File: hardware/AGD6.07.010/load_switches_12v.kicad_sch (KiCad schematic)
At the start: 0 parts

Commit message: Draw full AGD6.07.010 schematic per integrated_avionics_board spec
All ten sheets now carry components: 14S input with hot-swap and power
monitor, 12/5/3.3 V rails and a separate 12 V AI channel with soft-start
and current telemetry, Pixhawk connectors, CAN1/CAN2 hub with chokes,
ESD and switchable termination, sensor conditioning, SIYI and radar,
AI interface and watchdog, protected 12 V switches with diagnostics,
fan/heater control, cameras and Ethernet. Open choices are recorded in
DECISIONS.md; datasheet-dependent values are flagged CHECK_DATASHEET.

ERC: no errors. All 752 intended pin connections match the KiCad netlist.

Co-Authored-By: Claude Opus 5.5 <noreply@anthropic.com>
Claude-Session: https://claude.ai/code/session_01Qk7uTKdi6YbndB9fGuguYV
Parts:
- added C804, C811, C821, C831: 100n, Capacitor_SMD:C_0402_1005Metric, symbol Device:C
- added C805: 10u 25V, Capacitor_SMD:C_1210_3225Metric, symbol Device:C
- added D801, D802, D803, D804, D805: SS14, Diode_SMD:D_SMA, symbol Diode:SS14
- added D806: ESD9B5.0ST5G, Diode_SMD:D_SOD-923, symbol Diode:ESD9B5.0ST5G
- added D807: BAT54C, Package_TO_SOT_SMD:SOT-23, symbol Diode:BAT54C
- added F801: 0.5A, Fuse:Fuse_1206_3216Metric, symbol Device:Polyfuse
- added F802: 1.5A, Fuse:Fuse_1812_4532Metric, symbol Device:Polyfuse
- added J801: VALVE1 XH2, Connector_JST:JST_XH_B2B-XH-A_1x02_P2.50mm_Vertical, symbol Connector_Generic:Conn_01x02
- added J802: VALVE2 XH2, Connector_JST:JST_XH_B2B-XH-A_1x02_P2.50mm_Vertical, symbol Connector_Generic:Conn_01x02
- added J803: LIGHTS XH2, Connector_JST:JST_XH_B2B-XH-A_1x02_P2.50mm_Vertical, symbol Connector_Generic:Conn_01x02
- added J804: FAN XH2, Connector_JST:JST_XH_B2B-XH-A_1x02_P2.50mm_Vertical, symbol Connector_Generic:Conn_01x02
- added J805: HEATER XH2, Connector_JST:JST_XH_B2B-XH-A_1x02_P2.50mm_Vertical, symbol Connector_Generic:Conn_01x02
- added J806: PUMP_ESC_SIG GH3, Connector_JST:JST_GH_SM03B-GHS-TB_1x03-1MP_P1.25mm_Horizontal, symbol Connector_Generic:Conn_01x03
- added Q801, Q803: AO3400A, Package_TO_SOT_SMD:SOT-23, symbol Transistor_FET:AO3400A
- added Q802: AO3401A, Package_TO_SOT_SMD:SOT-23, symbol Transistor_FET:AO3401A
- added R804, R811, R821, R831: 4.7k, Resistor_SMD:R_0402_1005Metric, symbol Device:R
- added R805, R842, R852: 100k, Resistor_SMD:R_0402_1005Metric, symbol Device:R
- added R806: 22k, Resistor_SMD:R_0402_1005Metric, symbol Device:R
- added R807, R813, R823, R833: 10k, Resistor_SMD:R_0402_1005Metric, symbol Device:R
- added R812, R822, R832: 1.2k, Resistor_SMD:R_0402_1005Metric, symbol Device:R
- added R841, R851, R861: 100, Resistor_SMD:R_0402_1005Metric, symbol Device:R
- added TP801: ADC_RDY, TestPoint:TestPoint_Pad_D1.5mm, symbol Connector:TestPoint
- added U801, U802, U803: BTS5030-1EJA, Package_SO:Infineon_PG-DSO-8-43, symbol Power_Management:BTS5030-1EJA
- added U804: ADS1115IDGSR, Package_SO:TSSOP-10_3x3mm_P0.5mm, symbol Analog_ADC:ADS1115IDGS
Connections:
- new net +12V: C805.1, F801.1, F802.1, R805.1, U801.9 (VS), U802.9 (VS), U803.9 (VS)
- new net +3V3: C804.1, Q802.2 (S), R804.1, R807.1, U804.1 (ADDR), U804.8 (VDD)
- new net ADC_RDY: R807.2, TP801.1, U804.2 (ALERT/RDY)
- new net ALERT_DRV: D807.2, Q802.3 (D)
- new net DEN: R804.2, U801.3 (DEN), U802.3 (DEN), U803.3 (DEN)
- new net FAN_CTL: R841.1
- new net FAN_CTL_R: D807.1, R841.2
- new net FAN_G: D807.3, Q801.1 (G), R842.1
- new net FAN_N: D804.2 (A), J804.2 (Pin_2), Q801.3 (D)
- new net GND: C804.2, C805.2, C811.2, C821.2, C831.2, D801.2 (A), D802.2 (A), D803.2 (A), D806.2 (A2), J801.2 (Pin_2), J802.2 (Pin_2), J803.2 (Pin_2), J806.3 (Pin_3), Q801.2 (S), Q803.2 (S), R806.2, R812.2, R822.2, R832.2, R842.2, R852.2, U801.1 (GND), U802.1 (GND), U803.1 (GND), U804.3 (GND)
- new net HEATER_CTL: R851.1
- new net HEAT_G: Q803.1 (G), R851.2, R852.1
- new net HEAT_N: D805.2 (A), J805.2 (Pin_2), Q803.3 (D)
- new net I2C_SCL: U804.10 (SCL)
- new net I2C_SDA: U804.9 (SDA)
- new net IN1: R811.2, U801.2 (IN)
- new net IN2: R821.2, U802.2 (IN)
- new net IN3: R831.2, U803.2 (IN)
- new net IS1: R812.1, R813.1, U801.4 (IS)
- new net IS1_F: C811.1, R813.2, U804.4 (AIN0)
- new net IS2: R822.1, R823.1, U802.4 (IS)
- new net IS2_F: C821.1, R823.2, U804.5 (AIN1)
- new net IS3: R832.1, R833.1, U803.4 (IS)
- new net IS3_F: C831.1, R833.2, U804.6 (AIN2)
- new net LIGHTS_CTL: R831.1
- new net OUT1: D801.1 (K), J801.1 (Pin_1), U801.6 (OUT), U801.7 (OUT), U801.8 (OUT)
- new net OUT2: D802.1 (K), J802.1 (Pin_1), U802.6 (OUT), U802.7 (OUT), U802.8 (OUT)
- new net OUT3: D803.1 (K), J803.1 (Pin_1), U803.6 (OUT), U803.7 (OUT), U803.8 (OUT)
- new net PUMP_C: D806.1 (A1), J806.2 (Pin_2), R861.2
- new net PUMP_PWM: R861.1
- new net TEMP_ALERT_N: Q802.1 (G)
- new net V12_FAN: D804.1 (K), F801.2, J804.1 (Pin_1)
- new net V12_HEAT: D805.1 (K), F802.2, J805.1 (Pin_1)
- new net V12_MON: R805.2, R806.1, U804.7 (AIN3)
- new net VALVE1_CTL: R811.1
- new net VALVE2_CTL: R821.1
- no-connect marks 0 -> 4
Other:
- note added: "Ключи 12 V: 2 клапана, огни; вентилятор, нагреватель; сигнал насоса"
- note added: "ТРИ ЗАЩИЩЁННЫХ КЛЮЧА 12 V (ТЗ п. 1): U801/U802 — клапаны 1, 2; U803 — огни. BTS5030-1EJA: защита от КЗ и перегрева, диагностика обрыва/КЗ по току IS -> АЦП U804 ADS1115 (I2C 0x49) -> Pixhawk/ИИ. Обратные диоды SS14 на каждом выходе. Порог входа IN от 3.3 V логики Pixhawk и номинал R_IS — CHECK_DATASHEET. ВЕНТИЛЯТОР (ТЗ п. 5): включается программно (FAN_CTL, AUX5) ИЛИ аппаратно при перегреве (TEMP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"
- note removed: "DATA_REQUIRED: число клапанов форсунок и их ток"
- note removed: "Возвратные токи клапанов не проходят под аналоговой частью CAN_AND_SENSORS"
- note removed: "Ключи 12 V: клапаны форсунок, навигационные огни и anti-collision, вентилятор, зуммер"
- note removed: "Обратные диоды / TVS на каждой индуктивной нагрузке, контроль тока ключей"
- note removed: "Перенос схемы бывшего модуля ключей 12 V (исходник DATA_REQUIRED)"
- company: (none) -> АГД6.07.010
- title: (none) -> LOAD_SWITCHES_12V

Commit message: AGD6.07.010 rev 0.3: design review fixes and bring-up plan
Design review (DESIGN_REVIEW.md) with fixes applied to the schematic:
INA228 input RC filters, 12 V bus current monitor (INA228 0x45),
BTS5030 diagnostic scaling with clamp diodes, flow input level fix,
CAN1 changed from star to daisy chain with on-board terminator, AI
shutdown request, board buzzer, series resistors and ESD on external
I2C probes. Connectors merged so every connector sits on a board edge.
Adds calculations.md (power, IPC-2221 widths, hot-swap, thermal, ADC
scaling, CAN, clearances) and BRINGUP.md (step-by-step test plan).
ERC: no errors; all 820 intended pin connections verified. Board is
re-placed; routing in progress.

Co-Authored-By: Claude Opus 5.5 <noreply@anthropic.com>
Claude-Session: https://claude.ai/code/session_01Qk7uTKdi6YbndB9fGuguYV
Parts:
- removed J806: PUMP_ESC_SIG GH3, Connector_JST:JST_GH_SM03B-GHS-TB_1x03-1MP_P1.25mm_Horizontal, symbol Connector_Generic:Conn_01x03
- added BZ801: 12V active buzzer, Buzzer_Beeper:Buzzer_12x9.5RM7.6, symbol Device:Buzzer
- added D808: SS14, Diode_SMD:D_SMA, symbol Diode:SS14
- added D809: ESD9B5.0ST5G, Diode_SMD:D_SOD-923, symbol Diode:ESD9B5.0ST5G
- added D811, D812, D813: BAT54S, Package_TO_SOT_SMD:SOT-23, symbol Diode:BAT54S
- added J806: PUMP_PWM + CAM_TRIG GH4, Connector_JST:JST_GH_SM04B-GHS-TB_1x04-1MP_P1.25mm_Horizontal, symbol Connector_Generic:Conn_01x04
- added Q804: AO3400A, Package_TO_SOT_SMD:SOT-23, symbol Transistor_FET:AO3400A
- added R862, R871: 100, Resistor_SMD:R_0402_1005Metric, symbol Device:R
- added R872: 100k, Resistor_SMD:R_0402_1005Metric, symbol Device:R
- R812, R822, R832: value 1.2k -> 470
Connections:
- net +12V: now also BZ801.1 (+), D808.1 (K)
- net +3V3: now also D811.2 (K), D812.2 (K), D813.2 (K)
- net GND: now also D809.2 (A2), D811.1 (A), D812.1 (A), D813.1 (A), J806.3 (Pin_3), J806.4 (Pin_4), Q804.2 (S), R872.2
- net IS1_F: now also D811.3 (COM)
- net IS2_F: now also D812.3 (COM)
- net IS3_F: now also D813.3 (COM)
- net PUMP_C: now also J806.1 (Pin_1)
- new net BUZZER_CTL: R871.1
- new net BUZ_G: Q804.1 (G), R871.2, R872.1
- new net BUZ_N: BZ801.2 (-), D808.2 (A), Q804.3 (D)
- new net CAM_TRIG: R862.1
- new net TRIG_C: D809.1 (A1), J806.2 (Pin_2), R862.2
- no-connect marks 4 -> 3

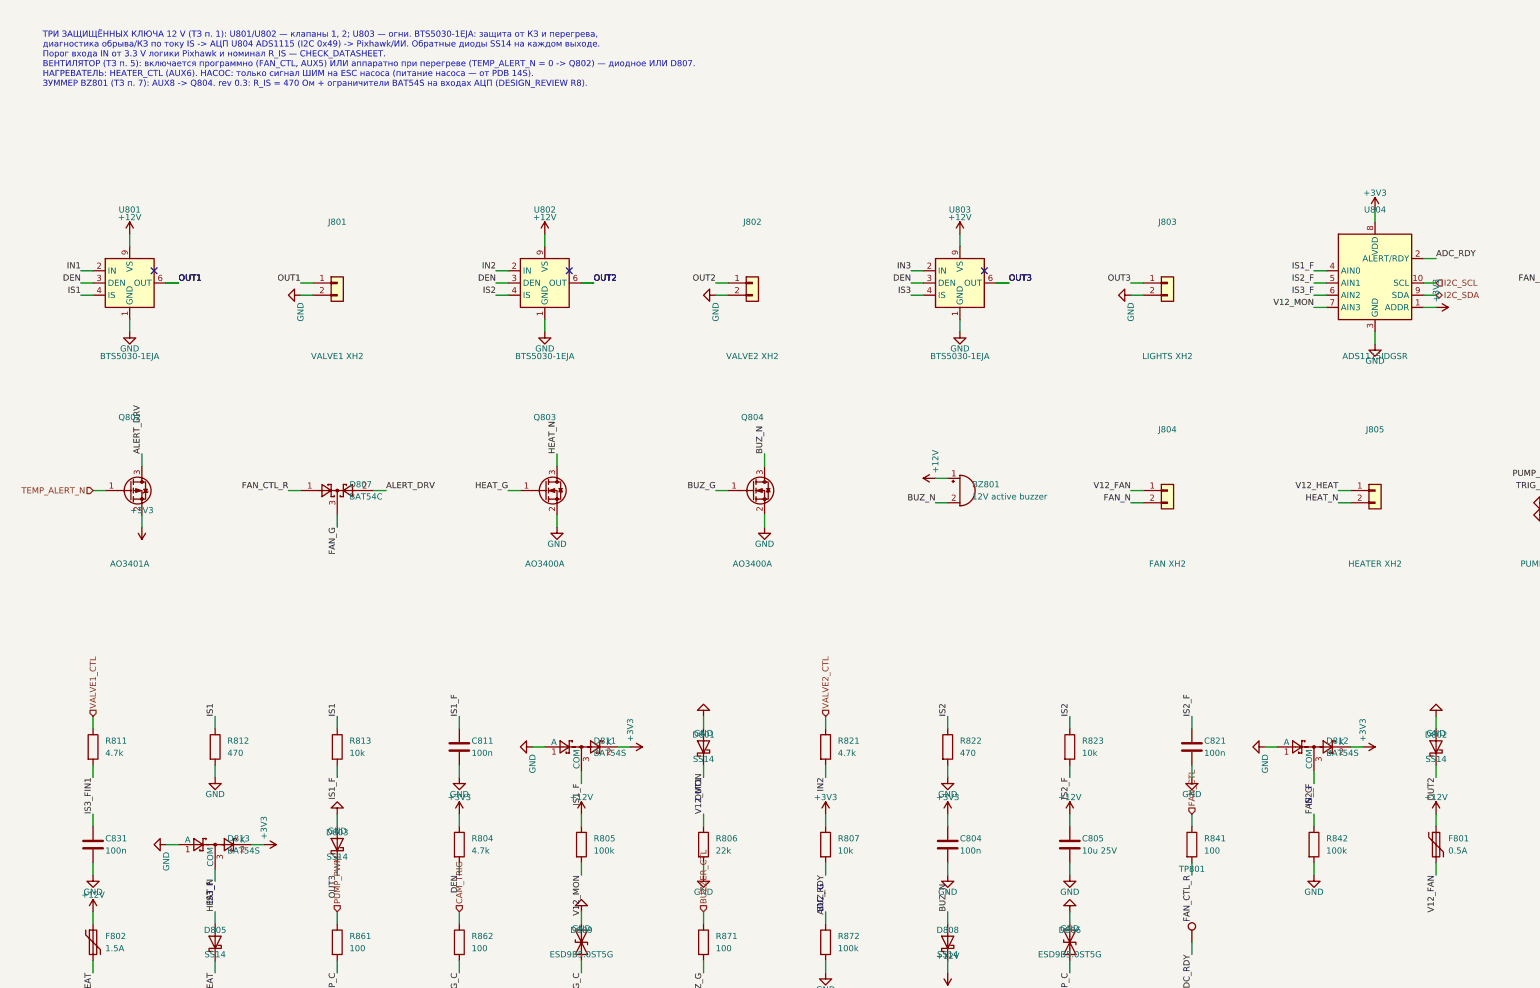
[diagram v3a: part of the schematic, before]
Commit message: AGD6.07.010 rev 0.4 (WIP): 3x TRACO THL40 DC/DC, split 12 V bus, SwitchBlox Ethernet, fixed LM5069 UVLO/OVLO, computed hot-swap values, PX4 firmware notes; board re-placed, routing in progress
Co-Authored-By: Claude Opus 5.5 <noreply@anthropic.com>
Claude-Session: https://claude.ai/code/session_01Qk7uTKdi6YbndB9fGuguYV
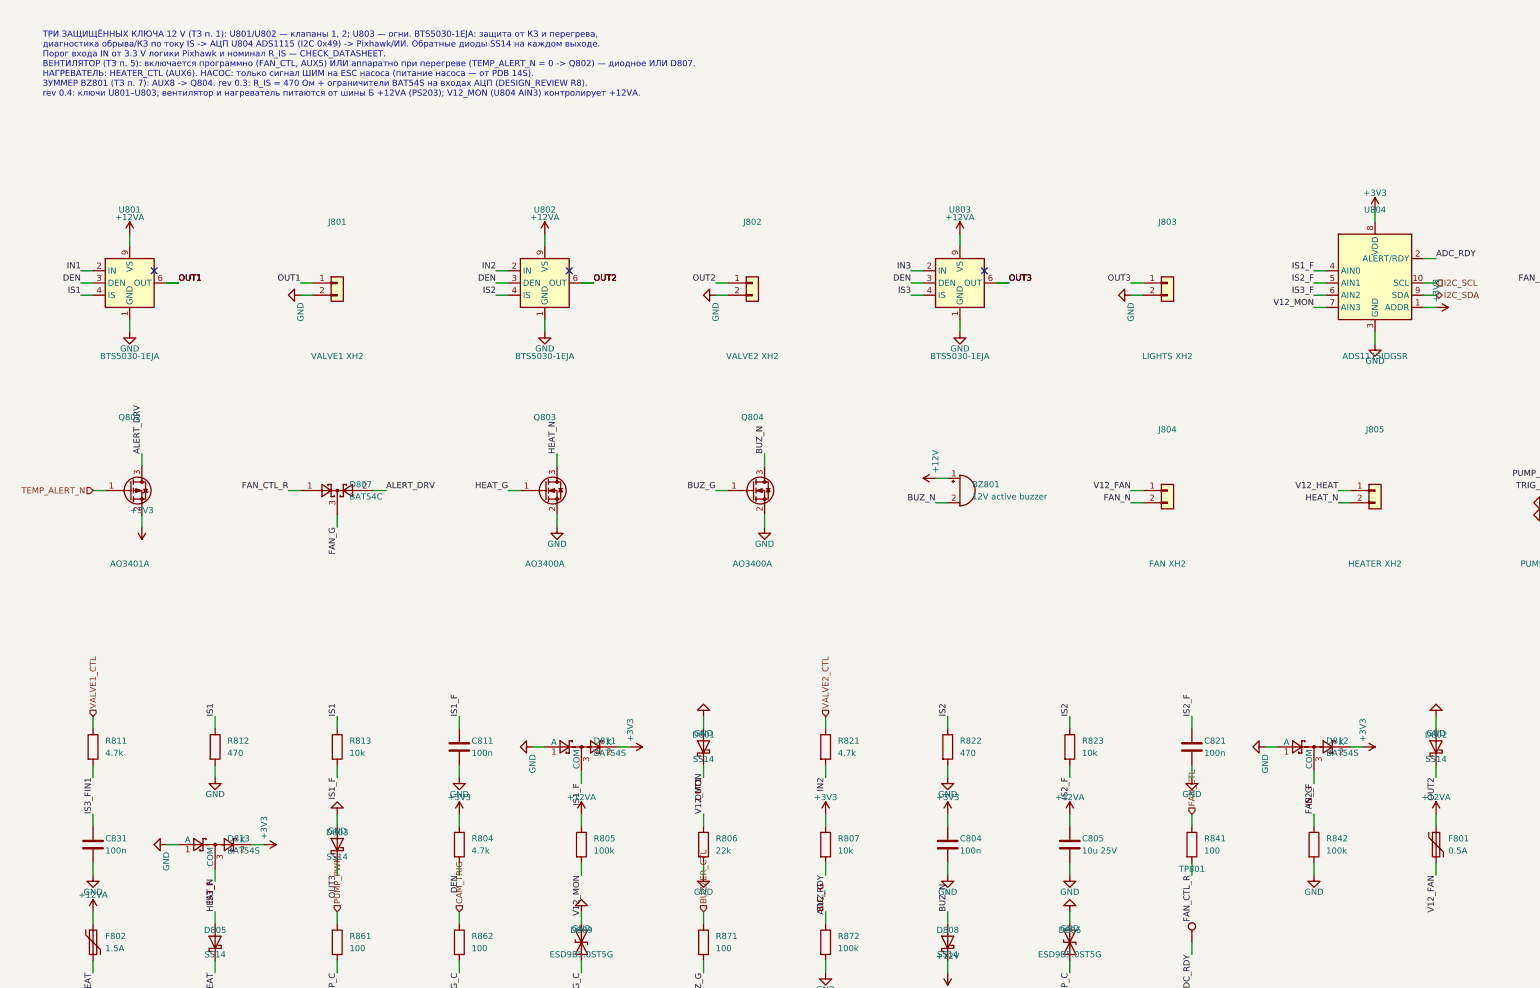
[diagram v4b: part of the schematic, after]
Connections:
- net +12V: no longer C805.1, F801.1, F802.1, R805.1, U801.9 (VS), U802.9 (VS), U803.9 (VS)
- new net +12VA: C805.1, F801.1, F802.1, R805.1, U801.9 (VS), U802.9 (VS), U803.9 (VS)
